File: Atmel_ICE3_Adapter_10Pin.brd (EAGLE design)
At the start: 17.4 x 19.5 mm, 2 parts

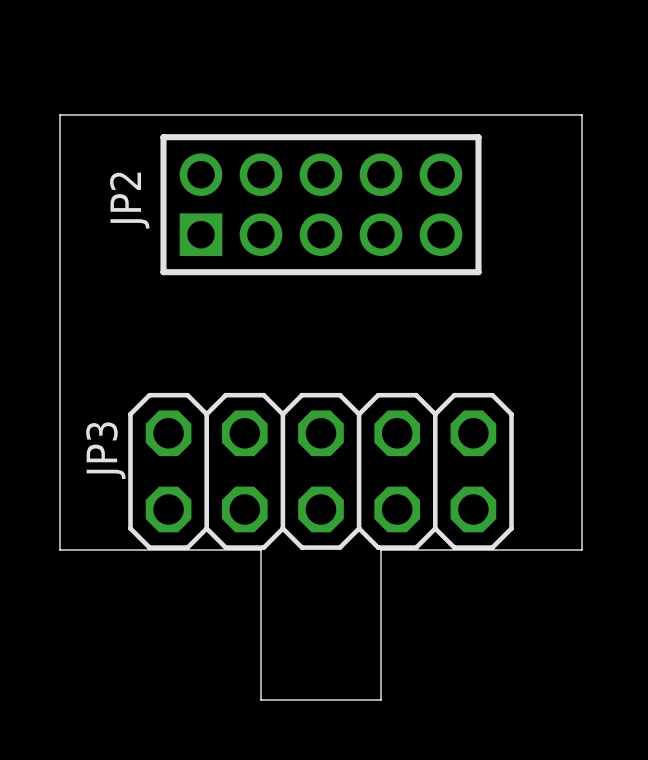
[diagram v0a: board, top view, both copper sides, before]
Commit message: Fix 6 pin wrong ICE3 header
Add 10 pin
Add gerber files
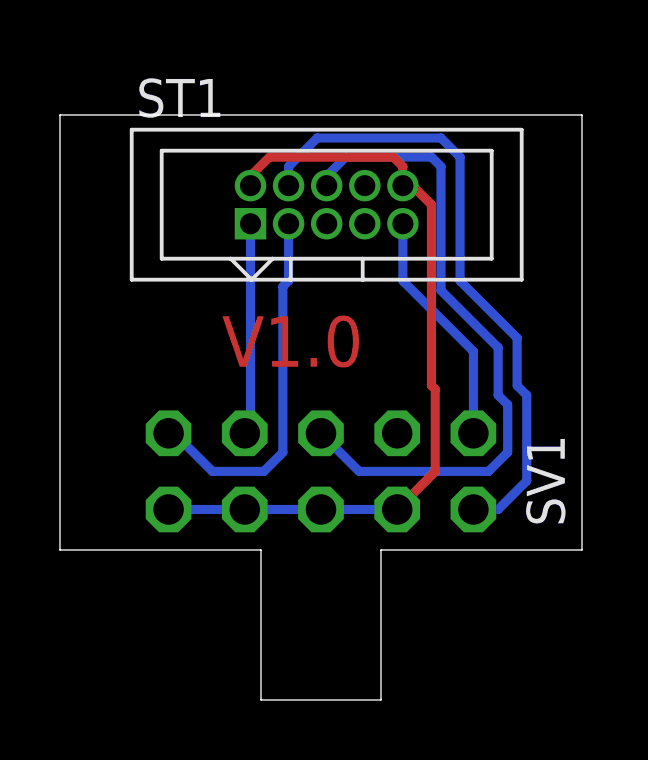
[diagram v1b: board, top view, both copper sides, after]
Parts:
- removed JP2: (no value), pinhead_2:2X05M
- removed JP3: (no value), pinhead_2:2X05
- added ST1: MA05-2_WANNE, pin-header-1.27:MA05-2_WANNE
- added SV1: (no value), con-lstb:MA05-2
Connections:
- net !SRST: now also ST1.6, SV1.6; no longer JP2.6, JP3.5
- net !TRST: now also ST1.8; no longer JP2.8
- net GND: now also ST1.10, ST1.2, SV1.3, SV1.5, SV1.7, SV1.9; no longer JP2.10, JP2.2, JP3.10, JP3.4, JP3.6, JP3.8
- net TCK: now also ST1.1, SV1.8; no longer JP2.1, JP3.7
- net TDI: now also ST1.9, SV1.2; no longer JP2.9, JP3.1
- net TDO: now also ST1.3, SV1.10; no longer JP2.3, JP3.9
- net TMS: now also ST1.5; no longer JP2.5
- net VTG: now also ST1.4, SV1.1; no longer JP2.4, JP3.2
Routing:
- net GND: track 0.00 -> 26.0 mm
- net !SRST: track 0.00 -> 22.0 mm
- net VTG: track 0.00 -> 20.9 mm
- net TDO: track 0.00 -> 12.3 mm
- net TDI: track 0.00 -> 7.96 mm
- net TCK: track 0.00 -> 7.17 mm
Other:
- board text added: "V1.0"
